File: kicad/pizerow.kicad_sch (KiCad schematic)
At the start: 1 part

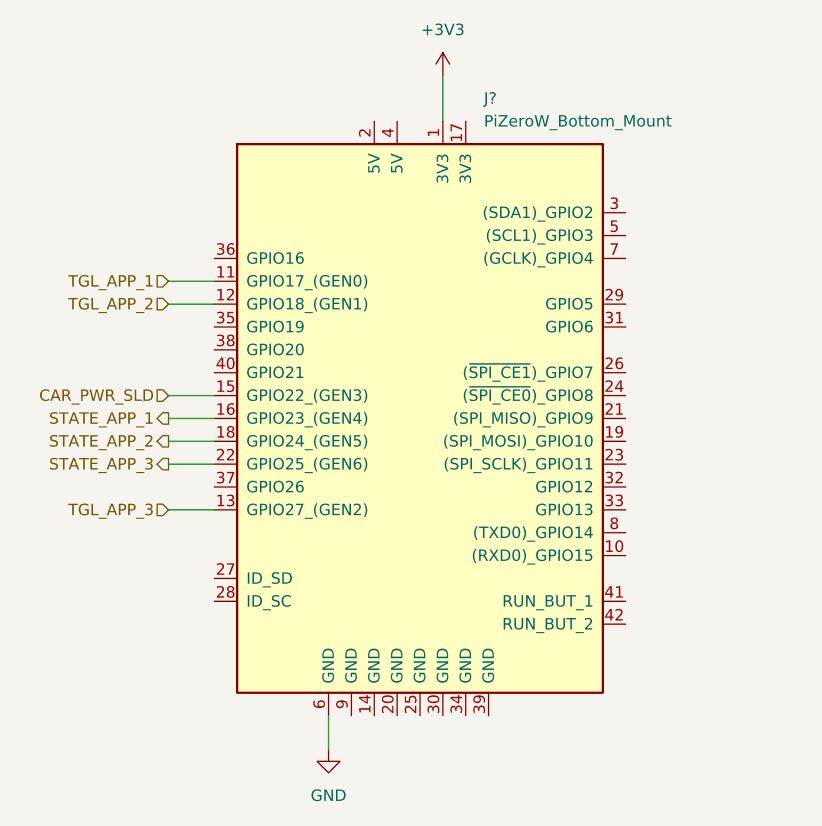
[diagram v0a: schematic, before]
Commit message: developed proper schematic in KiCad along with supporting firmware. code still doesnt gracefully handle all errors but it now does for ureq (network) errors, turning the LAN light off but not ejecting
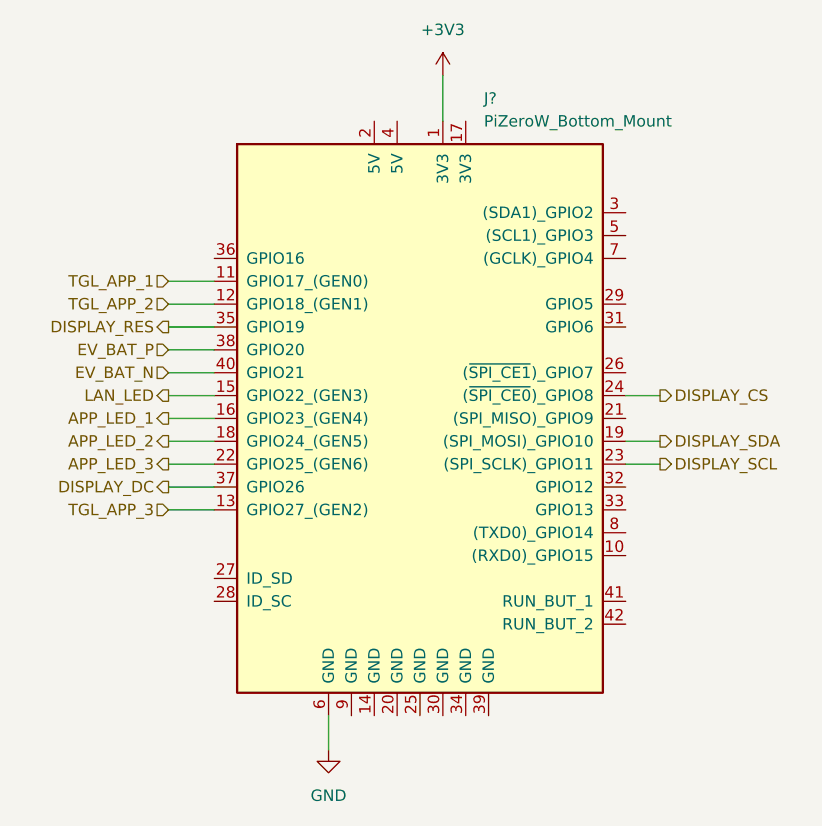
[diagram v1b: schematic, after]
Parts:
- J?: footprint PiZeroWLib:RBPiZero -> Connector_PinHeader_2.54mm:PinHeader_2x20_P2.54mm_Vertical
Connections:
- net DISPLAY_SDA: now reaches J?.19 ((SPI_MOSI)_GPIO10)
- net DISPLAY_SCL: now reaches J?.23 ((SPI_SCLK)_GPIO11)
- net DISPLAY_CS: now reaches J?.24 ((~{SPI_CE0})_GPIO8)
- net DISPLAY_RES: now reaches J?.35 (GPIO19)
- net DISPLAY_DC: now reaches J?.37 (GPIO26)
- net EV_BAT_P: now reaches J?.38 (GPIO20)
- net EV_BAT_N: now reaches J?.40 (GPIO21)
- net CAR_PWR_SLD renamed LAN_LED
- net STATE_APP_1 renamed APP_LED_1
- net STATE_APP_2 renamed APP_LED_2
- net STATE_APP_3 renamed APP_LED_3
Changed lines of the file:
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@@
-(kicad_sch (version 20211123) (generator eeschema)
+(kicad_sch (version 20230121) (generator eeschema)
   (paper "A4")
   (wire (pts (xy 121.92 53.34) (xy 121.92 58.42))
-    (stroke (width 0) (type default) (color 0 0 0 0))
+    (stroke (width 0) (type default))
+  )
+  (wire (pts (xy 142.24 96.52) (xy 146.05 96.52))
+    (stroke (width 0) (type default))
+  )
+  (wire (pts (xy 91.44 99.06) (xy 96.52 99.06))
+    (stroke (width 0) (type default))
   )
   (wire (pts (xy 91.44 76.2) (xy 96.52 76.2))
-    (stroke (width 0) (type default) (color 0 0 0 0))
+    (stroke (width 0) (type default))
+  )
+  (wire (pts (xy 91.44 81.28) (xy 96.52 81.28))
+    (stroke (width 0) (type default))
+  )
+  (wire (pts (xy 91.44 86.36) (xy 96.52 86.36))
+    (stroke (width 0) (type default))
   )
   (wire (pts (xy 91.44 88.9) (xy 96.52 88.9))
-    (stroke (width 0) (type default) (color 0 0 0 0))
+    (stroke (width 0) (type default))
+  )
+  (wire (pts (xy 142.24 88.9) (xy 146.05 88.9))
+    (stroke (width 0) (type default))
   )
   (wire (pts (xy 91.44 96.52) (xy 96.52 96.52))
-    (stroke (width 0) (type default) (color 0 0 0 0))
+    (stroke (width 0) (type default))
   )
   (wire (pts (xy 91.44 93.98) (xy 96.52 93.98))
-    (stroke (width 0) (type default) (color 0 0 0 0))
+    (stroke (width 0) (type default))
+  )
+  (wire (pts (xy 91.44 83.82) (xy 96.52 83.82))
+    (stroke (width 0) (type default))
   )
   (wire (pts (xy 91.44 101.6) (xy 96.52 101.6))
-    (stroke (width 0) (type default) (color 0 0 0 0))
+    (stroke (width 0) (type default))
   )
   (wire (pts (xy 91.44 78.74) (xy 96.52 78.74))
-    (stroke (width 0) (type default) (color 0 0 0 0))
+    (stroke (width 0) (type default))
+  )
+  (wire (pts (xy 142.24 93.98) (xy 146.05 93.98))
+    (stroke (width 0) (type default))
   )
   (wire (pts (xy 109.22 124.46) (xy 109.22 128.27))
-    (stroke (width 0) (type default) (color 0 0 0 0))
+    (stroke (width 0) (type default))
   )
   (wire (pts (xy 91.44 91.44) (xy 96.52 91.44))
-    (stroke (width 0) (type default) (color 0 0 0 0))
-  )
-  (hierarchical_label "TGL_APP_1" (shape input) (at 91.44 76.2 180)
-    (effects (font (size 1.27 1.27)) (justify right))
-  )
-  (hierarchical_label "STATE_APP_3" (shape output) (at 91.44 96.52 180)
-    (effects (font (size 1.27 1.27)) (justify right))
-  )
-  (hierarchical_label "TGL_APP_3" (shape input) (at 91.44 101.6 180)
-    (effects (font (size 1.27 1.27)) (justify right))
-  )
-  (hierarchical_label "CAR_PWR_SLD" (shape input) (at 91.44 88.9 180)
-    (effects (font (size 1.27 1.27)) (justify right))
-  )
-  (hierarchical_label "STATE_APP_1" (shape output) (at 91.44 91.44 180)
-    (effects (font (size 1.27 1.27)) (justify right))
-  )
-  (hierarchical_label "STATE_APP_2" (shape output) (at 91.44 93.98 180)
-    (effects (font (size 1.27 1.27)) (justify right))
-  )
-  (hierarchical_label "TGL_APP_2" (shape input) (at 91.44 78.74 180)
+    (stroke (width 0) (type default))
+  )
+  (hierarchical_label "TGL_APP_1" (shape input) (at 91.44 76.2 180) (fields_autoplaced)
+    (effects (font (size 1.27 1.27)) (justify right))
+  )
+  (hierarchical_label "DISPLAY_SDA" (shape output) (at 146.05 93.98 0) (fields_autoplaced)
+    (effects (font (size 1.27 1.27)) (justify left))
+  )
+  (hierarchical_label "APP_LED_3" (shape output) (at 91.44 96.52 180) (fields_autoplaced)
+    (effects (font (size 1.27 1.27)) (justify right))
+  )
+  (hierarchical_label "TGL_APP_3" (shape input) (at 91.44 101.6 180) (fields_autoplaced)
+    (effects (font (size 1.27 1.27)) (justify right))
+  )
+  (hierarchical_label "DISPLAY_CS" (shape output) (at 146.05 88.9 0) (fields_autoplaced)
+    (effects (font (size 1.27 1.27)) (justify left))
+  )
+  (hierarchical_label "DISPLAY_SCL" (shape output) (at 146.05 96.52 0) (fields_autoplaced)
+    (effects (font (size 1.27 1.27)) (justify left))
+  )
+  (hierarchical_label "DISPLAY_RES" (shape output) (at 91.44 81.28 180) (fields_autoplaced)
+    (effects (font (size 1.27 1.27)) (justify right))
+  )
+  (hierarchical_label "EV_BAT_N" (shape input) (at 91.44 86.36 180) (fields_autoplaced)
+    (effects (font (size 1.27 1.27)) (justify right))
+  )
+  (hierarchical_label "APP_LED_1" (shape output) (at 91.44 91.44 180) (fields_autoplaced)
+    (effects (font (size 1.27 1.27)) (justify right))
+  )
+  (hierarchical_label "DISPLAY_DC" (shape output) (at 91.44 99.06 180) (fields_autoplaced)
+    (effects (font (size 1.27 1.27)) (justify right))
+  )
+  (hierarchical_label "APP_LED_2" (shape output) (at 91.44 93.98 180) (fields_autoplaced)
+    (effects (font (size 1.27 1.27)) (justify right))
+  )
+  (hierarchical_label "EV_BAT_P" (shape input) (at 91.44 83.82 180) (fields_autoplaced)
+    (effects (font (size 1.27 1.27)) (justify right))
+  )
+  (hierarchical_label "TGL_APP_2" (shape input) (at 91.44 78.74 180) (fields_autoplaced)
+    (effects (font (size 1.27 1.27)) (justify right))
+  )
+  (hierarchical_label "LAN_LED" (shape output) (at 91.44 88.9 180) (fields_autoplaced)
     (effects (font (size 1.27 1.27)) (justify right))
   )
   (symbol (lib_id "RBPiZero:PiZeroW_Bottom_Mount") (at 119.38 91.44 0) (unit 1)
-    (in_bom yes) (on_board yes) (fields_autoplaced)
-    (property "Reference" "J?" (id 0) (at 126.4794 55.88 0)
+    (in_bom yes) (on_board yes) (dnp no) (fields_autoplaced)
+    (property "Reference" "J?" (at 126.4794 55.88 0)
       (effects (font (size 1.27 1.27)) (justify left))
     )
-    (property "Value" "PiZeroW_Bottom_Mount" (id 1) (at 126.4794 58.42 0)
+    (property "Value" "PiZeroW_Bottom_Mount" (at 126.4794 58.42 0)
       (effects (font (size 1.27 1.27)) (justify left))
     )
-    (property "Footprint" "PiZeroWLib:RBPiZero" (id 2) (at 144.78 59.69 0)
-      (effects (font (size 1.27 1.27)) hide)
-    )
-    (property "Datasheet" "" (id 3) (at 120.65 95.25 0)
+    (property "Footprint" "Connector_PinHeader_2.54mm:PinHeader_2x20_P2.54mm_Vertical" (at 144.78 59.69 0)
+      (effects (font (size 1.27 1.27)) hide)
+    )
+    (property "Datasheet" "" (at 120.65 95.25 0)
       (effects (font (size 1.27 1.27)) hide)
     )
@@
     (pin "8")
     (pin "9")
+    (instances
+      (project "project"
+        (path "/9538e4ed-27e6-4c37-b989-9859dc0d49e8/2dd0a78a-9f0b-40ca-9e75-57533d65983b"
+          (reference "J?") (unit 1)
+        )
+      )
+    )
   )
   (symbol (lib_id "power:GND") (at 109.22 128.27 0) (unit 1)
-    (in_bom yes) (on_board yes) (fields_autoplaced)
-    (property "Reference" "#PWR?" (id 0) (at 109.22 134.62 0)
-      (effects (font (size 1.27 1.27)) hide)
-    )
-    (property "Value" "GND" (id 1) (at 109.22 133.35 0))
-    (property "Footprint" "" (id 2) (at 109.22 128.27 0)
-      (effects (font (size 1.27 1.27)) hide)
-    )
-    (property "Datasheet" "" (id 3) (at 109.22 128.27 0)
+    (in_bom yes) (on_board yes) (dnp no) (fields_autoplaced)
+    (property "Reference" "#PWR?" (at 109.22 134.62 0)
+      (effects (font (size 1.27 1.27)) hide)
+    )
+    (property "Value" "GND" (at 109.22 133.35 0)
+      (effects (font (size 1.27 1.27)))
+    )
+    (property "Footprint" "" (at 109.22 128.27 0)
+      (effects (font (size 1.27 1.27)) hide)
+    )
+    (property "Datasheet" "" (at 109.22 128.27 0)
       (effects (font (size 1.27 1.27)) hide)
     )
     (pin "1")
+    (instances
+      (project "project"
+        (path "/9538e4ed-27e6-4c37-b989-9859dc0d49e8/2dd0a78a-9f0b-40ca-9e75-57533d65983b"
+          (reference "#PWR?") (unit 1)
+        )
+      )
+    )
   )
   (symbol (lib_id "power:+3V3") (at 121.92 53.34 0) (unit 1)
-    (in_bom yes) (on_board yes) (fields_autoplaced)
-    (property "Reference" "#PWR?" (id 0) (at 121.92 57.15 0)
-      (effects (font (size 1.27 1.27)) hide)
-    )
-    (property "Value" "+3V3" (id 1) (at 121.92 48.26 0))
-    (property "Footprint" "" (id 2) (at 121.92 53.34 0)
-      (effects (font (size 1.27 1.27)) hide)
-    )
-    (property "Datasheet" "" (id 3) (at 121.92 53.34 0)
+    (in_bom yes) (on_board yes) (dnp no) (fields_autoplaced)
+    (property "Reference" "#PWR?" (at 121.92 57.15 0)
+      (effects (font (size 1.27 1.27)) hide)
+    )
+    (property "Value" "+3V3" (at 121.92 48.26 0)
+      (effects (font (size 1.27 1.27)))
+    )
+    (property "Footprint" "" (at 121.92 53.34 0)
+      (effects (font (size 1.27 1.27)) hide)
+    )
+    (property "Datasheet" "" (at 121.92 53.34 0)
       (effects (font (size 1.27 1.27)) hide)
     )
     (pin "1")
+    (instances
+      (project "project"
+        (path "/9538e4ed-27e6-4c37-b989-9859dc0d49e8/2dd0a78a-9f0b-40ca-9e75-57533d65983b"
+          (reference "#PWR?") (unit 1)
+        )
+      )
+    )
   )
 )

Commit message: adjustments to design on kicad
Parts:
- gave numbers to parts that had none: 1
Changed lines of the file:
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@@
   (symbol (lib_id "RBPiZero:PiZeroW_Bottom_Mount") (at 119.38 91.44 0) (unit 1)
     (in_bom yes) (on_board yes) (dnp no) (fields_autoplaced)
-    (property "Reference" "J?" (at 126.4794 55.88 0)
+    (property "Reference" "J2" (at 126.4794 55.88 0)
       (effects (font (size 1.27 1.27)) (justify left))
     )
@@
       (project "project"
         (path "/9538e4ed-27e6-4c37-b989-9859dc0d49e8/2dd0a78a-9f0b-40ca-9e75-57533d65983b"
-          (reference "J?") (unit 1)
+          (reference "J2") (unit 1)
         )
       )
@@
   (symbol (lib_id "power:GND") (at 109.22 128.27 0) (unit 1)
     (in_bom yes) (on_board yes) (dnp no) (fields_autoplaced)
-    (property "Reference" "#PWR?" (at 109.22 134.62 0)
+    (property "Reference" "#PWR0104" (at 109.22 134.62 0)
       (effects (font (size 1.27 1.27)) hide)
     )
@@
       (project "project"
         (path "/9538e4ed-27e6-4c37-b989-9859dc0d49e8/2dd0a78a-9f0b-40ca-9e75-57533d65983b"
-          (reference "#PWR?") (unit 1)
+          (reference "#PWR0104") (unit 1)
         )
       )
@@
   (symbol (lib_id "power:+3V3") (at 121.92 53.34 0) (unit 1)
     (in_bom yes) (on_board yes) (dnp no) (fields_autoplaced)
-    (property "Reference" "#PWR?" (at 121.92 57.15 0)
+    (property "Reference" "#PWR0103" (at 121.92 57.15 0)
       (effects (font (size 1.27 1.27)) hide)
     )
@@
       (project "project"
         (path "/9538e4ed-27e6-4c37-b989-9859dc0d49e8/2dd0a78a-9f0b-40ca-9e75-57533d65983b"
-          (reference "#PWR?") (unit 1)
+          (reference "#PWR0103") (unit 1)
         )
       )

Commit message: completed board layout and passed drc
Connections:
- no-connect marks 0 -> 24

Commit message: routed pcb, only bom left to do
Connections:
- net +3V3: now also J2.17 (3V3)
- net GND: now also J2.14 (GND), J2.20 (GND), J2.25 (GND), J2.30 (GND), J2.34 (GND), J2.39 (GND), J2.9 (GND)
- no-connect marks 24 -> 16
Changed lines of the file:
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@@
 	(paper "A4")
+	(junction
+		(at 121.92 128.27)
+		(diameter 0)
+		(color 0 0 0 0)
+	)
+	(junction
+		(at 116.84 128.27)
+		(diameter 0)
+		(color 0 0 0 0)
+	)
+	(junction
+		(at 121.92 55.88)
+		(diameter 0)
+		(color 0 0 0 0)
+	)
+	(junction
+		(at 111.76 128.27)
+		(diameter 0)
+		(color 0 0 0 0)
+	)
+	(junction
+		(at 114.3 128.27)
+		(diameter 0)
+		(color 0 0 0 0)
+	)
+	(junction
+		(at 124.46 128.27)
+		(diameter 0)
+		(color 0 0 0 0)
+	)
 	(junction
 		(at 109.22 128.27)
@@
 		(color 0 0 0 0)
 	)
-	(no_connect
-		(at 119.38 124.46)
+	(junction
+		(at 119.38 128.27)
+		(diameter 0)
+		(color 0 0 0 0)
 	)
 	(no_connect
@@
 	)
 	(no_connect
-		(at 121.92 124.46)
-	)
-	(no_connect
 		(at 142.24 104.14)
 	)
@@
 	)
 	(no_connect
-		(at 127 124.46)
-	)
-	(no_connect
 		(at 114.3 58.42)
 	)
@@
 	)
 	(no_connect
-		(at 116.84 124.46)
-	)
-	(no_connect
-		(at 124.46 124.46)
-	)
-	(no_connect
-		(at 114.3 124.46)
-	)
-	(no_connect
-		(at 124.46 58.42)
-	)
-	(no_connect
 		(at 142.24 81.28)
 	)
 	(no_connect
-		(at 111.76 124.46)
-	)
-	(no_connect
 		(at 96.52 111.76)
 	)
@@
 	(wire
 		(pts
-			(xy 121.92 53.34) (xy 121.92 58.42)
+			(xy 121.92 53.34) (xy 121.92 55.88)
+		)
+		(stroke
+			(width 0)
+			(type default)
+		)
+	)
+	(wire
+		(pts
+			(xy 124.46 58.42) (xy 124.46 55.88)
+		)
+		(stroke
+			(width 0)
+			(type default)
+		)
+	)
+	(wire
+		(pts
+			(xy 127 124.46) (xy 127 128.27)
 		)
 		(stroke
@@
 	(wire
 		(pts
+			(xy 124.46 124.46) (xy 124.46 128.27)
+		)
+		(stroke
+			(width 0)
+			(type default)
+		)
+	)
+	(wire
+		(pts
+			(xy 111.76 128.27) (xy 109.22 128.27)
+		)
+		(stroke
+			(width 0)
+			(type default)
+		)
+	)
+	(wire
+		(pts
+			(xy 119.38 124.46) (xy 119.38 128.27)
+		)
+		(stroke
+			(width 0)
+			(type default)
+		)
+	)
+	(wire
+		(pts
 			(xy 91.44 99.06) (xy 96.52 99.06)
 		)
@@
 	(wire
 		(pts
+			(xy 116.84 124.46) (xy 116.84 128.27)
+		)
+		(stroke
+			(width 0)
+			(type default)
+		)
+	)
+	(wire
+		(pts
 			(xy 91.44 76.2) (xy 96.52 76.2)
 		)
@@
 	(wire
 		(pts
+			(xy 116.84 128.27) (xy 114.3 128.27)
+		)
+		(stroke
+			(width 0)
+			(type default)
+		)
+	)
+	(wire
+		(pts
+			(xy 124.46 55.88) (xy 121.92 55.88)
+		)
+		(stroke
+			(width 0)
+			(type default)
+		)
+	)
+	(wire
+		(pts
+			(xy 124.46 128.27) (xy 121.92 128.27)
+		)
+		(stroke
+			(width 0)
+			(type default)
+		)
+	)
+	(wire
+		(pts
 			(xy 91.44 88.9) (xy 96.52 88.9)
 		)
@@
 	(wire
 		(pts
+			(xy 119.38 128.27) (xy 116.84 128.27)
+		)
+		(stroke
+			(width 0)
+			(type default)
+		)
+	)
+	(wire
+		(pts
+			(xy 111.76 124.46) (xy 111.76 128.27)
+		)
+		(stroke
+			(width 0)
+			(type default)
+		)
+	)
+	(wire
+		(pts
 			(xy 142.24 88.9) (xy 146.05 88.9)
 		)
@@
 	(wire
 		(pts
+			(xy 127 128.27) (xy 124.46 128.27)
+		)
+		(stroke
+			(width 0)
+			(type default)
+		)
+	)
+	(wire
+		(pts
+			(xy 114.3 124.46) (xy 114.3 128.27)
+		)
+		(stroke
+			(width 0)
+			(type default)
+		)
+	)
+	(wire
+		(pts
+			(xy 121.92 124.46) (xy 121.92 128.27)
+		)
+		(stroke
+			(width 0)
+			(type default)
+		)
+	)
+	(wire
+		(pts
 			(xy 101.6 128.27) (xy 109.22 128.27)
 		)
@@
 	(wire
 		(pts
+			(xy 121.92 128.27) (xy 119.38 128.27)
+		)
+		(stroke
+			(width 0)
+			(type default)
+		)
+	)
+	(wire
+		(pts
 			(xy 109.22 124.46) (xy 109.22 128.27)
 		)
@@
 		(pts
 			(xy 91.44 91.44) (xy 96.52 91.44)
+		)
+		(stroke
+			(width 0)
+			(type default)
+		)
+	)
+	(wire
+		(pts
+			(xy 114.3 128.27) (xy 111.76 128.27)
+		)
+		(stroke
+			(width 0)
+			(type default)
+		)
+	)
+	(wire
+		(pts
+			(xy 121.92 55.88) (xy 121.92 58.42)
 		)
 		(stroke
@@
 		(fields_autoplaced yes)
 		(property "Reference" "J2"
-			(at 126.4794 55.88 0)
+			(at 126.6541 55.88 0)
 			(effects
 				(font
@@
 		)
 		(property "Value" "PiZeroW_Bottom_Mount"
-			(at 126.4794 58.42 0)
+			(at 126.6541 58.42 0)
 			(effects
 				(font
@@
 		)
 		(property "Value" "GND"
-			(at 109.22 133.35 0)
-			(effects
-				(font
-					(size 1.27 1.27)
-				)
+			(at 111.76 129.5399 0)
+			(effects
+				(font
+					(size 1.27 1.27)
+				)
+				(justify left)
 			)
 		)
@@
 			)
 		)
-		(property "Description" ""
+		(property "Description" "Power symbol creates a global label with name \"GND\" , ground"
 			(at 109.22 128.27 0)
 			(effects
@@
 		)
 		(property "Value" "+3V3"
-			(at 121.92 48.26 0)
-			(effects
-				(font
-					(size 1.27 1.27)
-				)
+			(at 124.46 52.0699 0)
+			(effects
+				(font
+					(size 1.27 1.27)
+				)
+				(justify left)
 			)
 		)
@@
 			)
 		)
-		(property "Description" ""
+		(property "Description" "Power symbol creates a global label with name \"+3V3\""
 			(at 121.92 53.34 0)
 			(effects

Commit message: kicad changes
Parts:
- J2: LCSC (none) -> C2685142
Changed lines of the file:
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@@
 		(on_board yes)
 		(dnp no)
-		(fields_autoplaced yes)
 		(property "Reference" "J2"
 			(at 126.6541 55.88 0)
@@
 			(at 119.38 91.44 0)
 			(effects
+				(font
+					(size 1.27 1.27)
+				)
+				(hide yes)
+			)
+		)
+		(property "LCSC" "C2685142"
+			(at 119.38 91.44 0)
+			(effects
